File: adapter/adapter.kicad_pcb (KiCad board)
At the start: 2 copper layers, 41.8 x 50.8 mm, 30 parts, among them J1 Serial, J2 Battery charge, J3 Ribbon, J4 Ribbon, J5 RGB, SW1 SW_SPST, SW3 SW_SPDT, U1 Dual MCU: RP2040 + nice!nano, U2 AP1603WG-7, U3 USBLC6-2P6

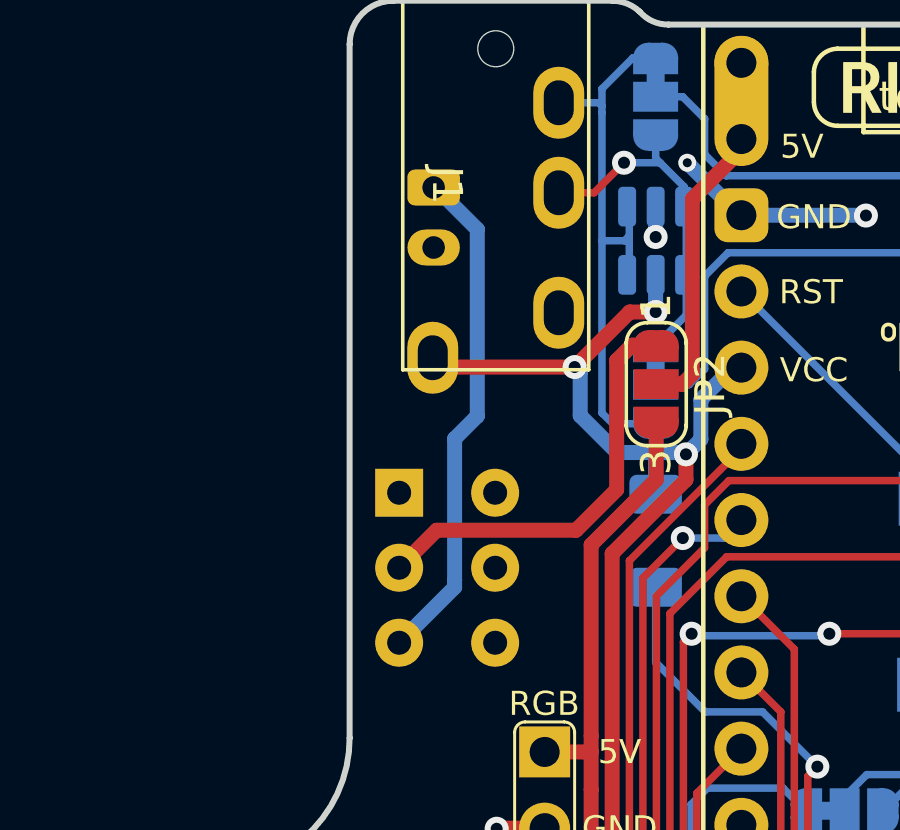
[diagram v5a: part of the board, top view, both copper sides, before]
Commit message: pcb: update the trrs footprint
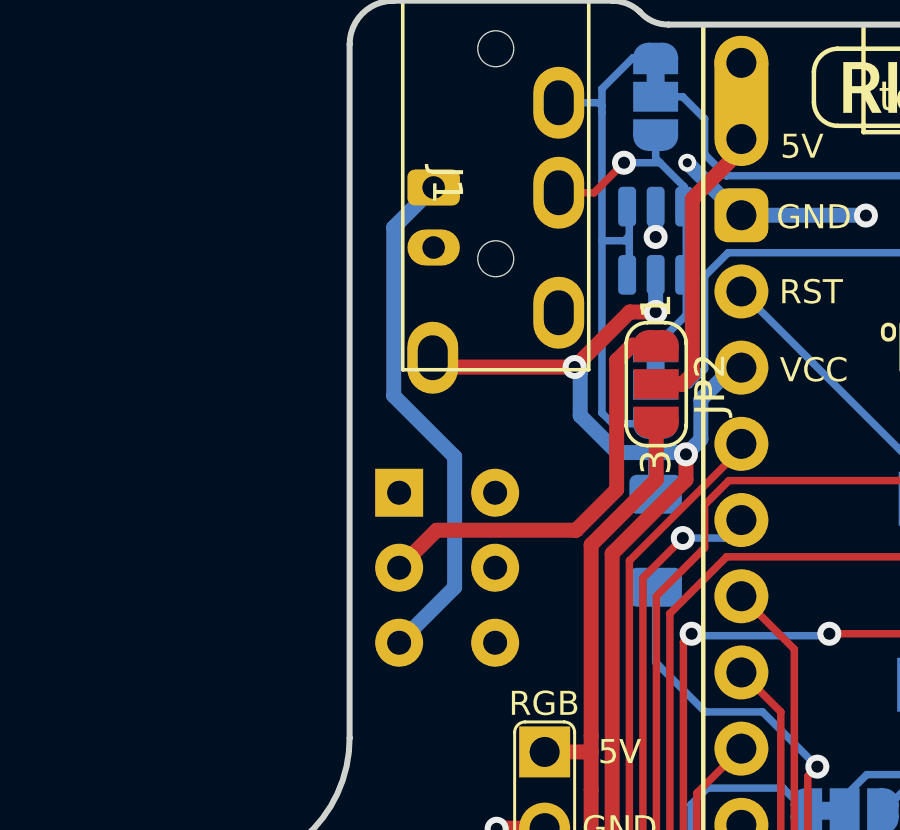
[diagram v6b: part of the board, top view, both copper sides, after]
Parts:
- J1: footprint library:CON_MJ-4PP-9-no-bottom-hole -> PCM_marbastlib-xp-various:CON_MJ-4PP-9
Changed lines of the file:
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@@
 		(fp_arc
 			(start 1 10.852513)
-			(mid 0.897486 11.099998)
+			(mid 0.897486 11.099999)
 			(end 0.65 11.202513)
 			(stroke
@@
 		(fp_arc
 			(start 1 10.852513)
-			(mid 0.897486 11.099998)
+			(mid 0.897486 11.099999)
 			(end 0.65 11.202513)
 			(stroke
@@
 		)
 	)
-	(footprint "library:CON_MJ-4PP-9-no-bottom-hole"
+	(footprint "PCM_marbastlib-xp-various:CON_MJ-4PP-9"
 		(layer "F.Cu")
 		(at 122.37 73.35 -90)
@@
 			)
 		)
-		(property "Footprint" "library:CON_MJ-4PP-9-no-bottom-hole"
+		(property "Footprint" "PCM_marbastlib-xp-various:CON_MJ-4PP-9"
 			(at 0 0 -90)
 			(unlocked yes)
@@
 		)
 		(fp_text user "${REFERENCE}"
-			(at 0 1.6 90)
+			(at 0 1.6 -90)
 			(layer "F.Fab")
 			(effects
@@
 			(layers "F&B.Cu" "*.Mask")
 		)
+		(pad "" np_thru_hole circle
+			(at 2.45 0)
+			(size 1.2 1.2)
+			(drill 1.2)
+			(layers "F&B.Cu" "*.Mask")
+		)
 		(pad "R1" thru_hole oval
 			(at 4.25 -2.1)
@@
 		(fp_arc
 			(start 1 5.802513)
-			(mid 0.897489 6.050001)
+			(mid 0.897489 6.050002)
 			(end 0.65 6.152513)
 			(stroke
@@
 		(fp_arc
 			(start 1 5.802513)
-			(mid 0.897489 6.050001)
+			(mid 0.897489 6.050002)
 			(end 0.65 6.152513)
 			(stroke
@@
 	)
 	(segment
-		(start 121 81.8)
-		(end 121 86.5)
-		(width 0.5)
-		(layer "B.Cu")
-		(net 16)
-	)
-	(segment
-		(start 121 81.8)
-		(end 121.755216 81.044784)
+		(start 119.15 88.6)
+		(end 121 86.75)
 		(width 0.5)
 		(layer "B.Cu")
@@
 	)
 	(segment
-		(start 121.755216 81.044784)
-		(end 121.755216 74.817716)
+		(start 121 82.4)
+		(end 118.97 80.37)
 		(width 0.5)
 		(layer "B.Cu")
@@
 	)
 	(segment
-		(start 121.755216 74.817716)
-		(end 120.3625 73.425)
+		(start 121 86.75)
+		(end 121 82.4)
 		(width 0.5)
 		(layer "B.Cu")
@@
 	)
 	(segment
-		(start 120.3625 73.425)
+		(start 118.97 74.755)
 		(end 120.3 73.425)
 		(width 0.5)
@@
 	)
 	(segment
-		(start 121 86.5)
-		(end 121 86.75)
-		(width 0.5)
-		(layer "B.Cu")
-		(net 16)
-	)
-	(segment
-		(start 121 86.75)
-		(end 119.15 88.6)
+		(start 118.97 80.37)
+		(end 118.97 74.755)
 		(width 0.5)
 		(layer "B.Cu")

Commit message: WIP - RECORD POSITIONS AND REVERT
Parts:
- moved U1 2.65 mm to (137.7, 81.9)
- moved JP3 2.54 mm to (134.0, 94.4)
- moved JP7 2.54 mm to (134.0, 91.7)
- moved SW1 2.54 mm to (138.2, 84.4)
- moved kibuzzard-61F01C84 2.54 mm to (142.1, 84.3)
- moved J2 2.07 mm to (119.9, 71.4)
- moved J1 1.88 mm to (121.8, 71.5)
- moved JP2 0.82 mm to (126.9, 80.0)
- moved JP1 0.80 mm to (126.9, 70.4)
- moved U3 0.80 mm to (126.9, 75.2)
- moved JP5 0.80 mm to (126.9, 80.0)
- moved R1 0.80 mm to (126.9, 85.2)
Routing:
- net SDA_L: track 46.5 -> 0.00 mm
- net MOSI_L: track 43.9 -> 0.00 mm, vias 2 -> 0
- net SCL_L: track 43.6 -> 0.00 mm
- net SCLK_L: track 41.0 -> 0.00 mm
- net col6_l: track 40.9 -> 0.00 mm
- net row5_l: track 40.4 -> 0.00 mm, vias 1 -> 0
- net MISO_L: track 37.9 -> 0.00 mm, vias 1 -> 0
- net GPIO_2_L: track 34.8 -> 0.00 mm
- net GPIO_1_L: track 32.0 -> 0.00 mm, vias 1 -> 0
- net RGB_L: track 27.1 -> 0.00 mm, vias 1 -> 0
- net col5_l: track 24.0 -> 0.00 mm
- net Net-(JP3-A): track 22.2 -> 0.00 mm, vias 2 -> 0
- net col1_l: track 21.4 -> 0.00 mm
- net row2_l: track 21.2 -> 0.00 mm
- net col2_l: track 20.1 -> 0.00 mm
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
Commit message: pcb: start redoing the PCB
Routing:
- net GND_L: track 5.83 -> 6.84 mm, vias 8 -> 9
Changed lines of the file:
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@@
+		(net 12)
+	)
+	(via
+		(at 126.898 75.085)
+		(size 0.8)
+		(drill 0.4)
+		(layers "F.Cu" "B.Cu")
 		(net 12)
 	)
@@
 		(layer "B.Cu")
 		(net 12)
+	)
+	(segment
+		(start 126.898053 75.085)
+		(end 126.898 75.084947)
+		(width 0.25)
+		(layer "B.Cu")
+		(net 12)
+	)
+	(segment
+		(start 126.898 75.084947)
+		(end 126.898 74.0725)
+		(width 0.25)
+		(layer "B.Cu")
+		(net 12)
